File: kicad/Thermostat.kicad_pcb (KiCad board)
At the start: 4 copper layers, 82 x 46 mm, 10 parts, among them J1 Conn_02x20_Odd_Even, J2 Conn_01x02, M3*6 MountingHole_3.2mm_M3, U3 XIAO-ESP32-C6-SMD

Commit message: final pcb
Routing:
- net GND: vias 1 -> 0
- net /VSENSE: vias 1 -> 0
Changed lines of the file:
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@@
 		(filling no)
 		(pcbplotparams
-			(layerselection 0x00000000_00000000_55555555_5755f5ff)
+			(layerselection 0x00000000_00000000_55555555_5755f5af)
 			(plot_on_all_layers_selection 0x00000000_00000000_00000000_00000000)
 			(disableapertmacros no)
-			(usegerberextensions no)
+			(usegerberextensions yes)
 			(usegerberattributes yes)
 			(usegerberadvancedattributes yes)
@@
 			(sketchdnponfab yes)
 			(crossoutdnponfab yes)
-			(subtractmaskfromsilk no)
+			(subtractmaskfromsilk yes)
 			(outputformat 1)
 			(mirror no)
-			(drillshape 1)
+			(drillshape 0)
 			(scaleselection 1)
-			(outputdirectory "")
+			(outputdirectory "gerbers/")
 		)
 	)
@@
 			)
 		)
-		(attr exclude_from_pos_files exclude_from_bom)
+		(attr board_only exclude_from_pos_files exclude_from_bom)
 		(duplicate_pad_numbers_are_jumpers no)
 		(fp_circle
@@
 		(at 101.5305 127.9317 180)
 		(property "Reference" "U3"
-			(at 7.112 -21.336 0)
+			(at 6.9305 -8.2683 0)
 			(layer "F.SilkS")
 			(effects
 				(font
-					(size 0.78232 0.78232)
+					(size 1 1)
 					(thickness 0.10668)
 				)
@@
 			)
 		)
-		(attr exclude_from_pos_files exclude_from_bom)
+		(attr board_only exclude_from_pos_files exclude_from_bom)
 		(duplicate_pad_numbers_are_jumpers no)
 		(fp_circle
@@
 		(fp_circle
 			(center 0 0)
-			(end 3 0)
+			(end 2.8 0)
 			(stroke
 				(width 0.05)
@@
 			)
 		)
-		(attr exclude_from_pos_files exclude_from_bom)
+		(attr board_only exclude_from_pos_files exclude_from_bom)
 		(duplicate_pad_numbers_are_jumpers no)
 		(fp_circle
@@
 			)
 		)
-		(attr exclude_from_pos_files exclude_from_bom)
+		(attr board_only exclude_from_pos_files exclude_from_bom)
 		(duplicate_pad_numbers_are_jumpers no)
 		(fp_circle
@@
 		(net "/VSENSE")
 	)
-	(via
-		(at 79.11 129.8)
-		(size 0.6)
-		(drill 0.3)
-		(layers "F.Cu" "B.Cu")
-		(net "/VSENSE")
-	)
 	(segment
 		(start 79.11 129.8)
@@
 		(net "GND")
 	)
-	(via
-		(at 104.84 111.74)
-		(size 0.6)
-		(drill 0.3)
-		(layers "F.Cu" "B.Cu")
-		(net "GND")
-	)
 	(segment
 		(start 90.8795 110.6995)
@@
 			)
 		)
-	)
-	(zone
-		(net "GND")
-		(layers "F.Cu" "B.Cu")
-		(hatch edge 0.5)
-		(priority 1)
-		(connect_pads
-			(clearance 0.5)
-		)
-		(min_thickness 0.25)
-		(fill yes
-			(thermal_gap 0.5)
-			(thermal_bridge_width 0.5)
-			(island_removal_mode 0)
-		)
-		(polygon
-			(pts
-				(xy 65.9 100.5) (xy 66 151) (xy 155 150.9) (xy 154.9 100.3)
-			)
-		)

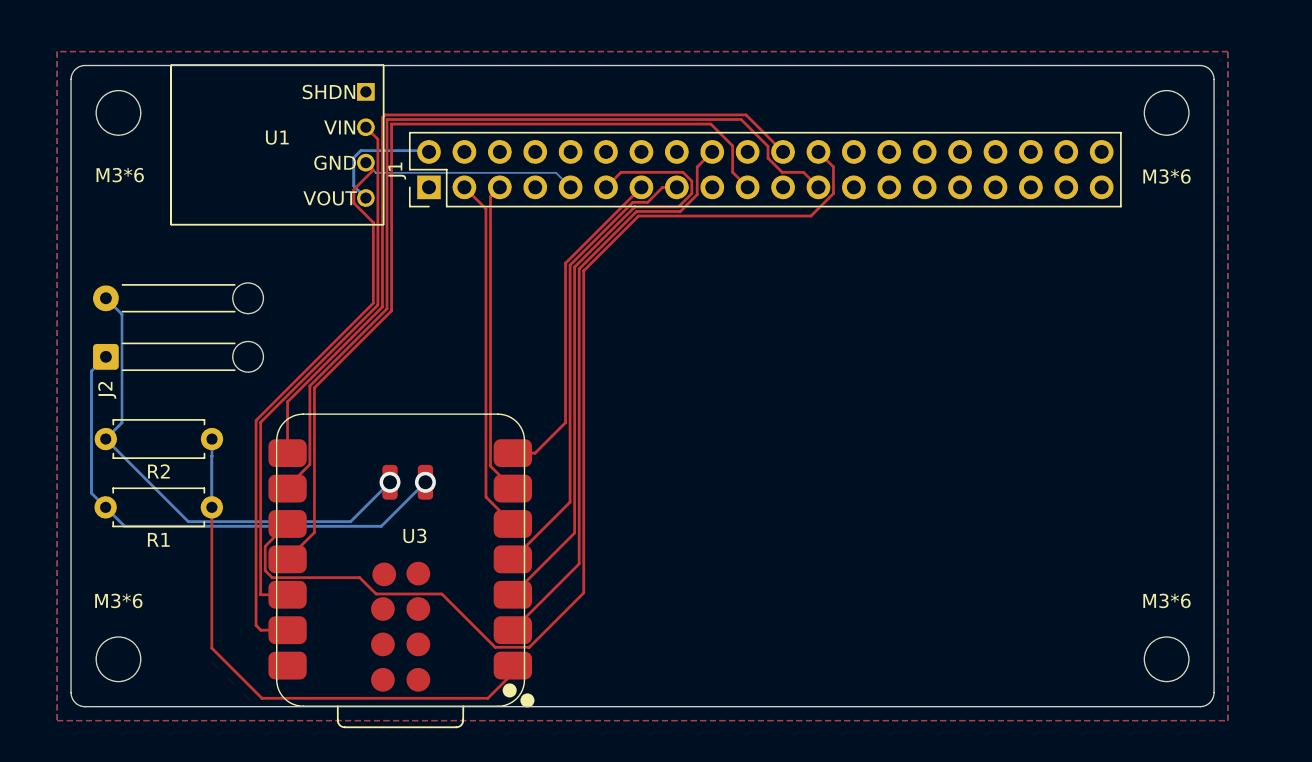
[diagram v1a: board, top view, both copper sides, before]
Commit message: fix dimensions
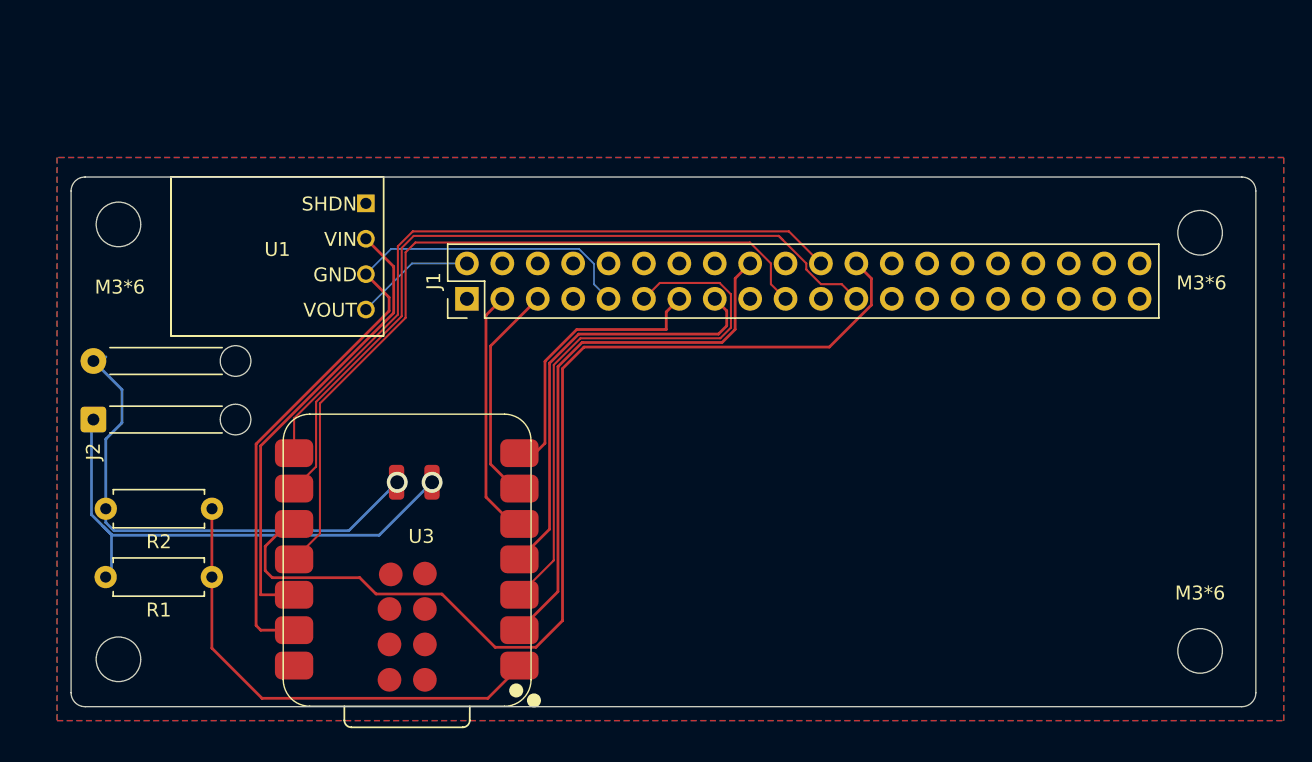
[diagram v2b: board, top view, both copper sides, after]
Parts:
- moved M3*6 8.93 mm to (150.0, 115.0)
- moved J1 8.45 mm to (97.4, 119.7)
- moved M3*6 8.00 mm to (72.4, 114.4)
- moved U1 8.00 mm to (83.8, 116.7)
- moved R1 5.00 mm to (79.1, 139.7)
- moved R2 5.00 mm to (79.1, 134.8)
- moved J2 4.59 mm to (70.6, 128.4)
- moved M3*6 2.47 mm to (150.0, 145.0)
- moved U3 0.47 mm to (102.0, 127.9)
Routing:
- net /SDA: track 25.6 -> 17.9 mm
- net /MOSI: track 62.9 -> 55.4 mm
- net /DC: track 56.8 -> 49.7 mm
- net /CLK: track 62.9 -> 56.1 mm
- net /3V3: track 39.3 -> 32.7 mm
- net /SCL: track 22.6 -> 16.1 mm
- net /VSENSE: track 39.4 -> 35.2 mm
- net /CS: track 77.5 -> 74.0 mm
- net GND: track 56.3 -> 53.2 mm
- net /BSY: track 42.1 -> 39.0 mm
- net /RST: track 43.7 -> 40.8 mm
- net /INT: track 23.8 -> 21.8 mm
- net -BATT: track 35.1 -> 37.0 mm
- net /TCH_RST: track 32.8 -> 31.1 mm
- net +BATT: track 36.5 -> 37.6 mm
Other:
- board size 82 x 46 mm -> 85 x 38 mm
